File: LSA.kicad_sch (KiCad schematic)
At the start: 0 parts

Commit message: 3D models.
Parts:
- added J1, J2: 685119248123, Mustang_Library:685119248123, symbol 685119248123:685119248123

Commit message: Place and align PCB components to enclosure DXF. Expand PCB 15mm both sides of USB-C. Move BM83 to right side. Cutout PCB along right side for antenna function.
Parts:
- J1, J2: symbol 685119248123:685119248123 -> Mustang_Library:685119248123
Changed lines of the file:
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@@
 	)
 	(symbol
-		(lib_id "685119248123:685119248123")
+		(lib_id "Mustang_Library:685119248123")
 		(at 176.53 137.16 0)
 		(unit 1)
@@
 	)
 	(symbol
-		(lib_id "685119248123:685119248123")
+		(lib_id "Mustang_Library:685119248123")
 		(at 179.07 232.41 0)
 		(unit 1)

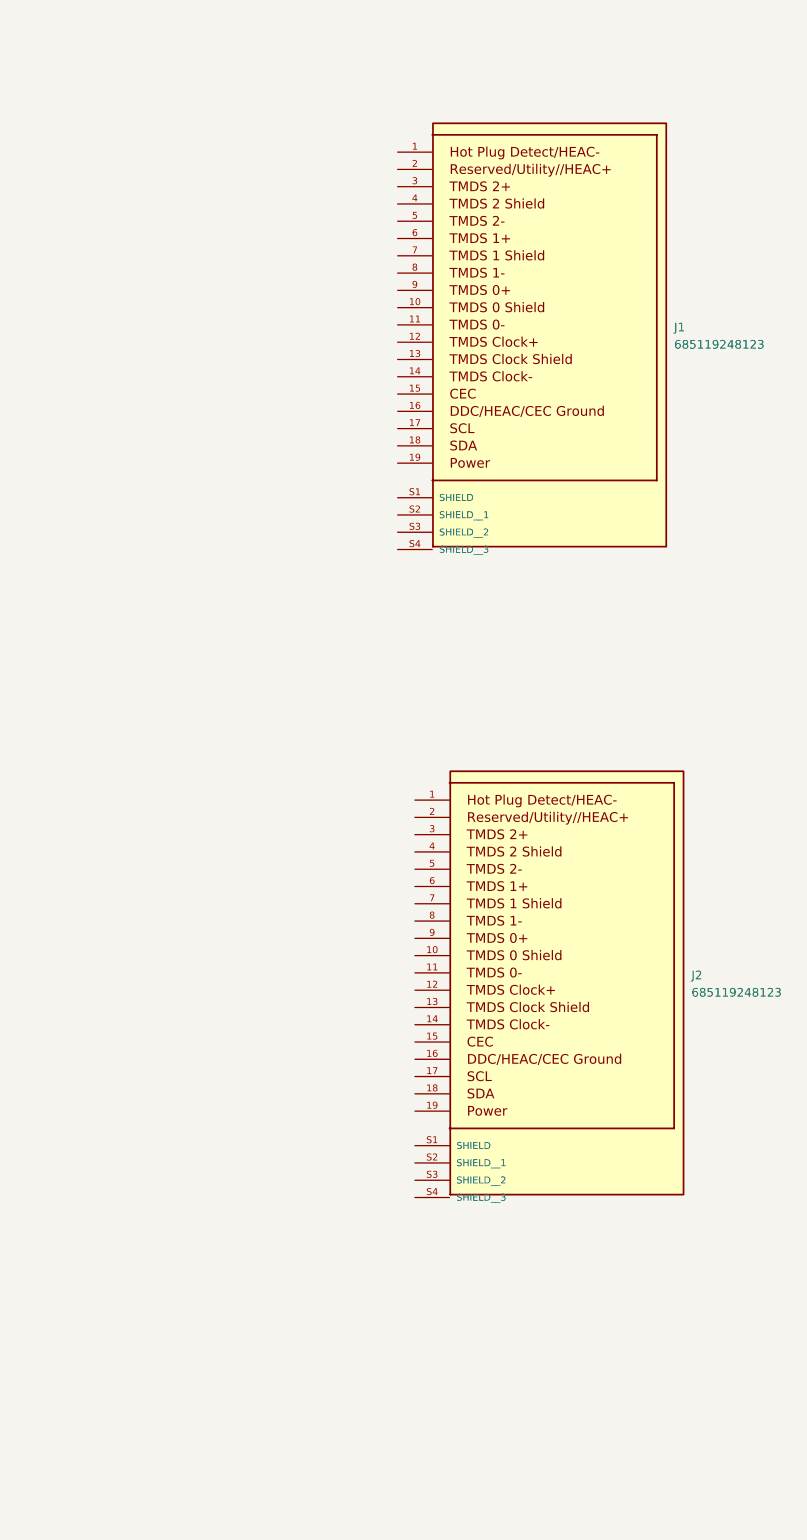
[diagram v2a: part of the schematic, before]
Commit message: Footprint inspections and cleanups.
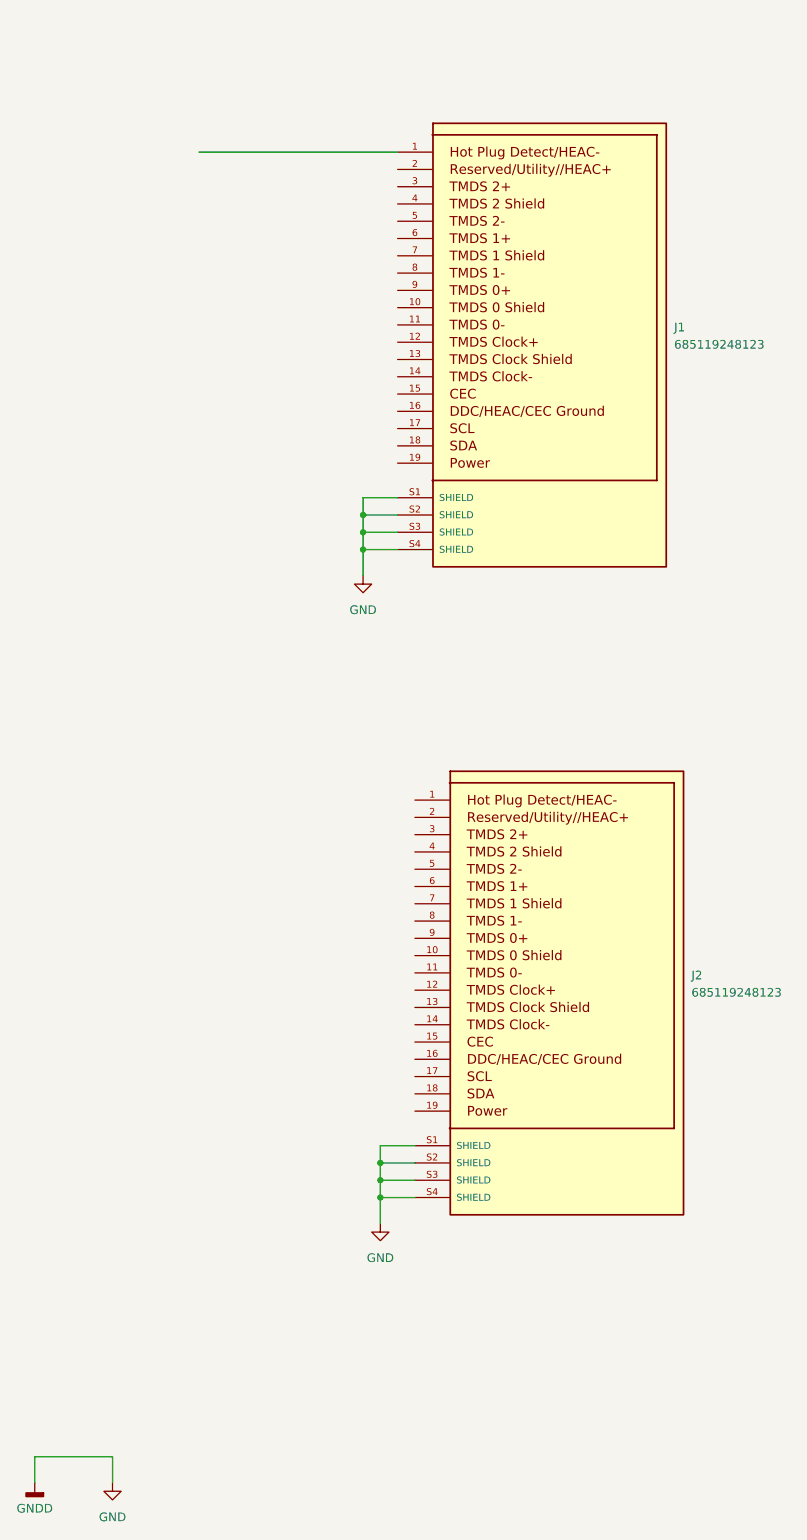
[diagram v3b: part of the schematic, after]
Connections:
- net GND: now reaches J1.S1 (SHIELD)
- net GND: now also J1.S2 (SHIELD), J1.S3 (SHIELD), J1.S4 (SHIELD), J2.S1 (SHIELD), J2.S2 (SHIELD), J2.S3 (SHIELD), J2.S4 (SHIELD)
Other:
- moved on the sheet: J1, J2

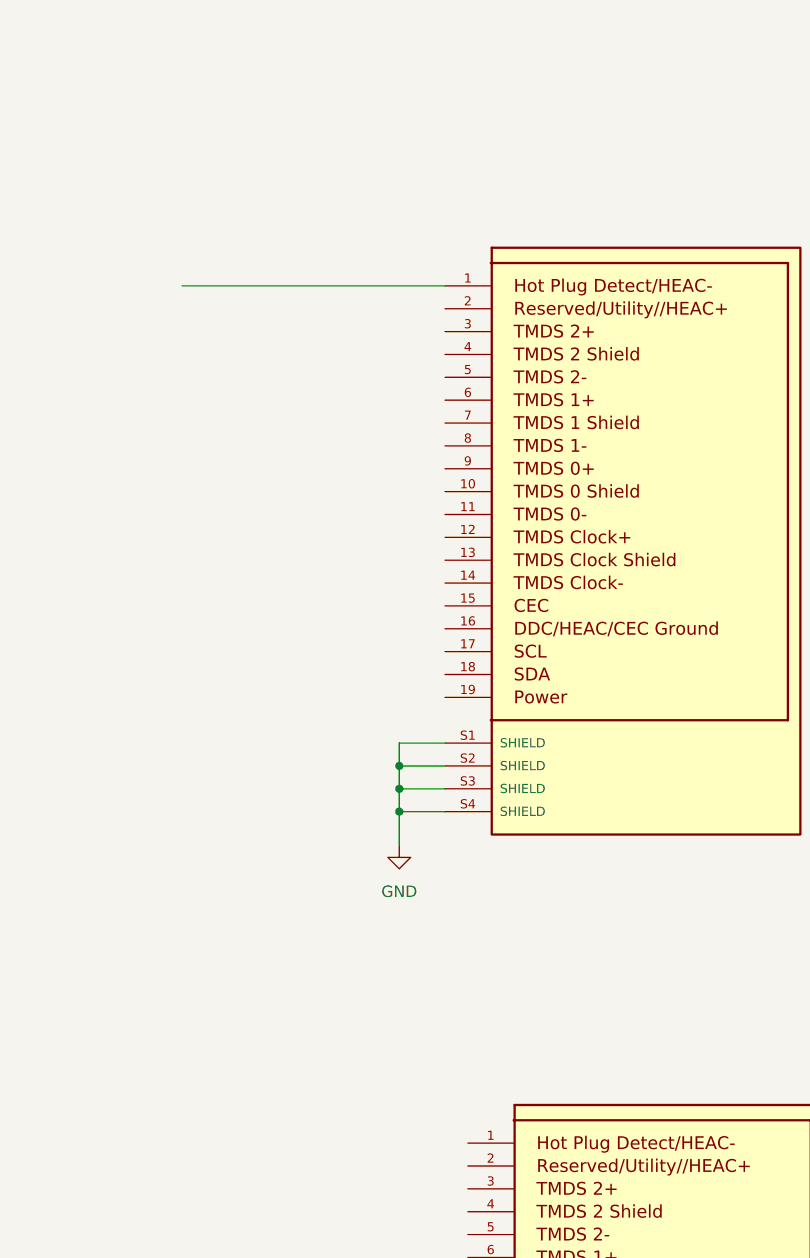
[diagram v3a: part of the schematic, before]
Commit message: Add extra mounting hole. Relocate BM83 per Juan.
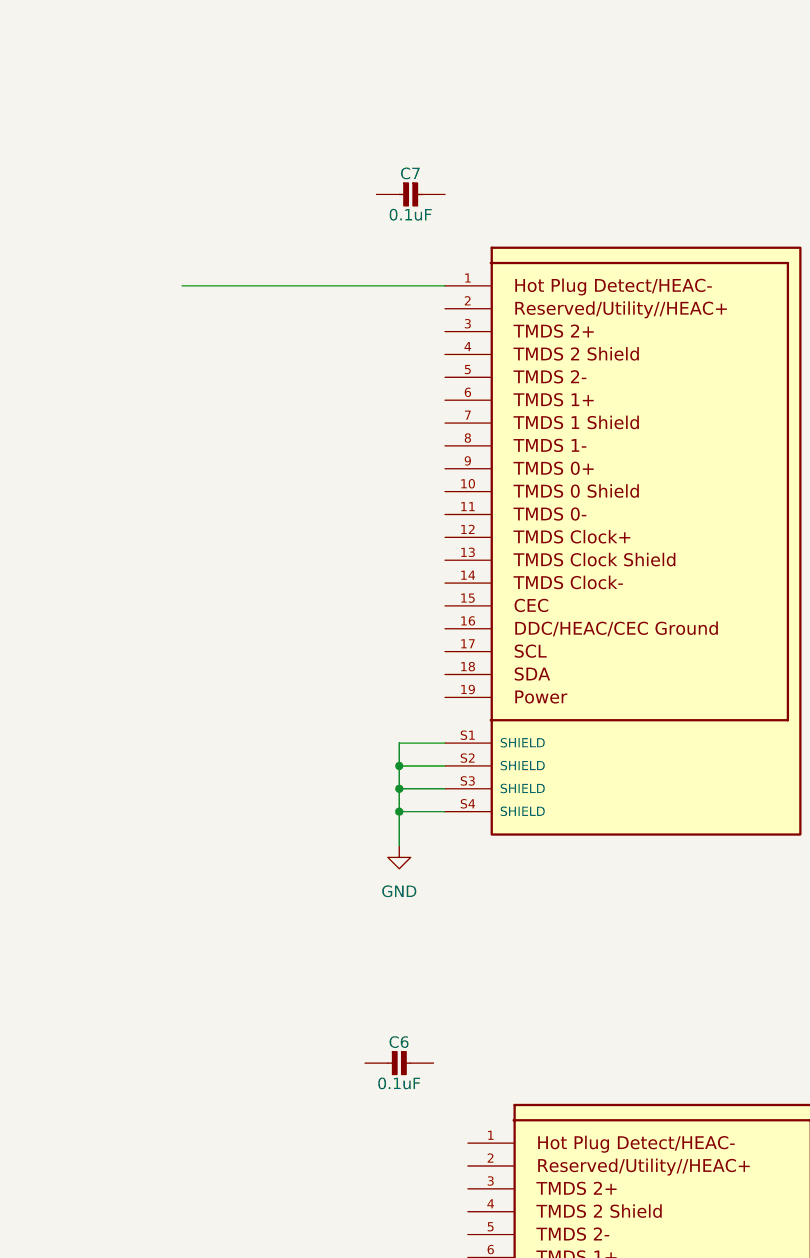
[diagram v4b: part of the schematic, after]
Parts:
- added C6, C7: 0.1uF, Mustang_Library:C_0805_2012Metric_Pad1.18x1.45mm_HandSolder, symbol Mustang_Library:CAP_CERAMIC0805-NOOUTLINE
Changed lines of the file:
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@@
+	)
+	(symbol
+		(lib_id "Mustang_Library:CAP_CERAMIC0805-NOOUTLINE")
+		(at 149.86 200.66 270)
+		(unit 1)
+		(exclude_from_sim no)
+		(in_bom yes)
+		(on_board yes)
+		(dnp no)
+		(property "Reference" "C6"
+			(at 151.11 198.37 90)
+			(effects
+				(font
+					(size 1.27 1.27)
+				)
+			)
+		)
+		(property "Value" "0.1uF"
+			(at 151.11 202.96 90)
+			(effects
+				(font
+					(size 1.27 1.27)
+				)
+			)
+		)
+		(property "Footprint" "Mustang_Library:C_0805_2012Metric_Pad1.18x1.45mm_HandSolder"
+			(at 149.86 200.66 0)
+			(effects
+				(font
+					(size 1.27 1.27)
+				)
+				(hide yes)
+			)
+		)
+		(property "Datasheet" ""
+			(at 149.86 200.66 0)
+			(effects
+				(font
+					(size 1.27 1.27)
+				)
+				(hide yes)
+			)
+		)
+		(property "Description" "Ceramic Capacitors\n\nFor new designs, use the packages preceded by an '_' character since they are more reliable:\n\nThe following footprints should be used on most boards:\n\n• _0402 - Standard footprint for regular board layouts\n• _0603 - Standard footprint for regular board layouts\n• _0805 - Standard footprint for regular board layouts\n• _1206 - Standard footprint for regular board layouts\n\nFor extremely tight-pitch boards where space is at a premium, the following 'micro-pitch' footprints can be used (smaller pads, no silkscreen outline, etc.):\n\n• _0402MP - Micro-pitch footprint for very dense/compact boards\n• _0603MP - Micro-pitch footprint for very dense/compact boards\n• _0805MP - Micro-pitch footprint for very dense/compact boards\n• _1206MP - Micro-pitch footprint for very dense/compact boards"
+			(at 149.86 200.66 0)
+			(effects
+				(font
+					(size 1.27 1.27)
+				)
+				(hide yes)
+			)
+		)
+		(pin "2"
+		)
+		(pin "1"
+		)
+		(instances
+			(project "Mustang-Digital"
+				(path "/5e27fdeb-580f-476f-92aa-43cee2f9d9cd/65eefc28-c8b5-4fa6-a61a-e7b5d07fd6b9"
+					(reference "C6")
+					(unit 1)
+				)
+			)
+		)
 	)
 	(symbol
@@
 					(unit 1)
 				)
+			)
+		)
+	)
+	(symbol
+		(lib_id "Mustang_Library:CAP_CERAMIC0805-NOOUTLINE")
+		(at 151.13 104.14 270)
+		(unit 1)
+		(exclude_from_sim no)
+		(in_bom yes)
+		(on_board yes)
+		(dnp no)
+		(property "Reference" "C7"
+			(at 152.38 101.85 90)
+			(effects
+				(font
+					(size 1.27 1.27)
+				)
+			)
+		)
+		(property "Value" "0.1uF"
+			(at 152.38 106.44 90)
+			(effects
+				(font
+					(size 1.27 1.27)
+				)
+			)
+		)
+		(property "Footprint" "Mustang_Library:C_0805_2012Metric_Pad1.18x1.45mm_HandSolder"
+			(at 151.13 104.14 0)
+			(effects
+				(font
+					(size 1.27 1.27)
+				)
+				(hide yes)
+			)
+		)
+		(property "Datasheet" ""
+			(at 151.13 104.14 0)
+			(effects
+				(font
+					(size 1.27 1.27)
+				)
+				(hide yes)
+			)
+		)
+		(property "Description" "Ceramic Capacitors\n\nFor new designs, use the packages preceded by an '_' character since they are more reliable:\n\nThe following footprints should be used on most boards:\n\n• _0402 - Standard footprint for regular board layouts\n• _0603 - Standard footprint for regular board layouts\n• _0805 - Standard footprint for regular board layouts\n• _1206 - Standard footprint for regular board layouts\n\nFor extremely tight-pitch boards where space is at a premium, the following 'micro-pitch' footprints can be used (smaller pads, no silkscreen outline, etc.):\n\n• _0402MP - Micro-pitch footprint for very dense/compact boards\n• _0603MP - Micro-pitch footprint for very dense/compact boards\n• _0805MP - Micro-pitch footprint for very dense/compact boards\n• _1206MP - Micro-pitch footprint for very dense/compact boards"
+			(at 151.13 104.14 0)
+			(effects
+				(font
+					(size 1.27 1.27)
+				)
+				(hide yes)
+			)
+		)
+		(pin "2"
+		)
+		(pin "1"
+		)
+		(instances
+			(project "Mustang-Digital"
+				(path "/5e27fdeb-580f-476f-92aa-43cee2f9d9cd/65eefc28-c8b5-4fa6-a61a-e7b5d07fd6b9"
+					(reference "C7")
+					(unit 1)
+				)
